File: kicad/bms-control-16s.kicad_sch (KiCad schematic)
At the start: 18 parts, among them J1 RJ45, J2 UEXT, J3 USB_B_Micro, J4 RJ45, J5 Conn_02x09_Top_Bottom

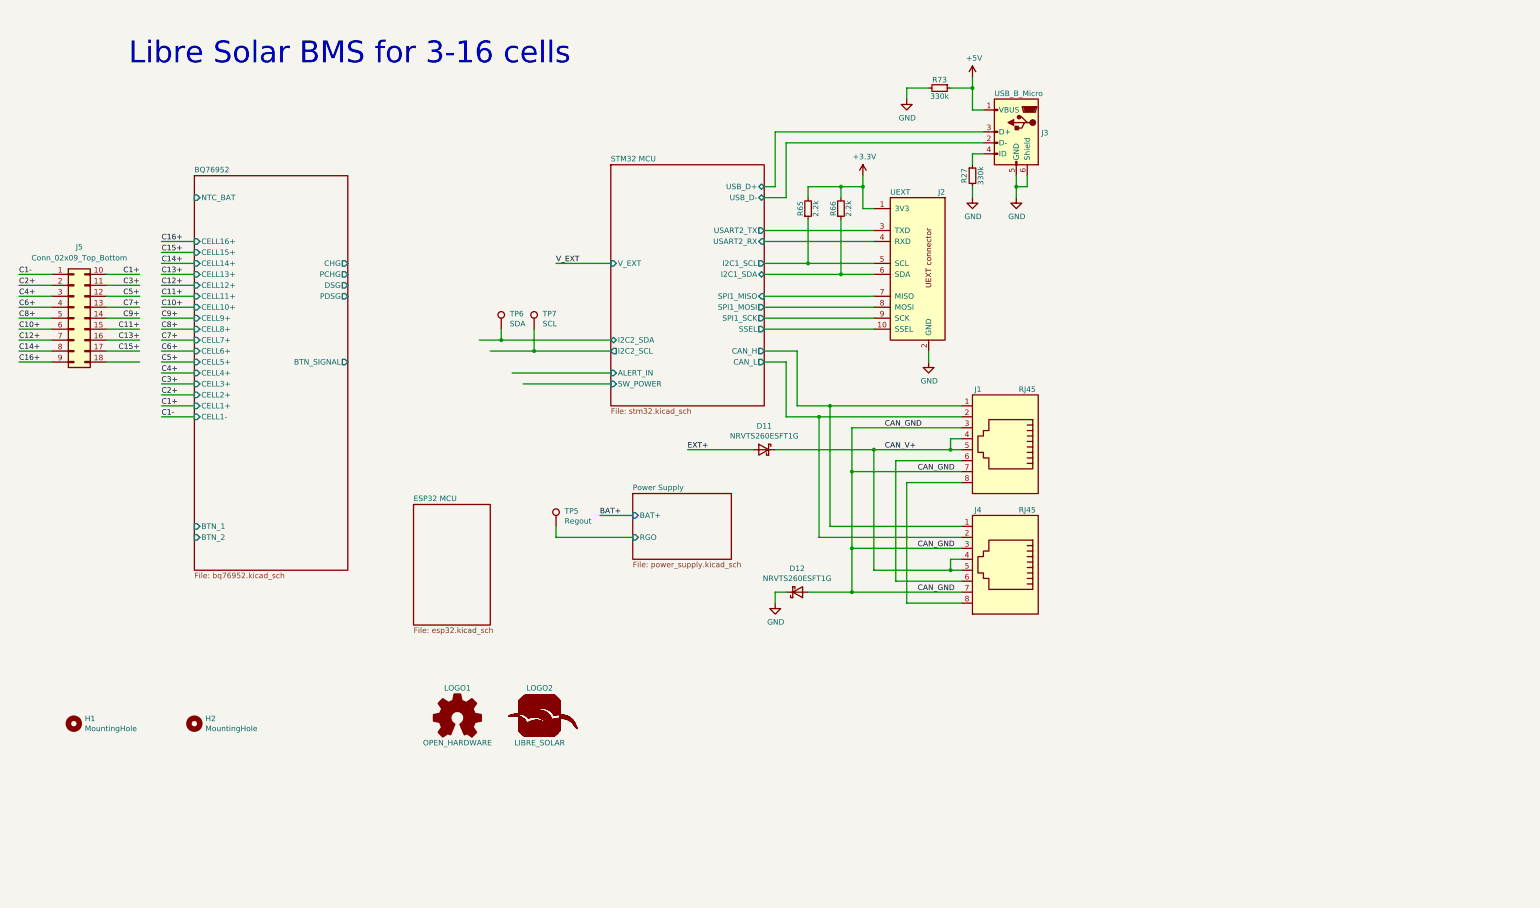
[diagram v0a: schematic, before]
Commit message: Update KiCad files based on spec updates
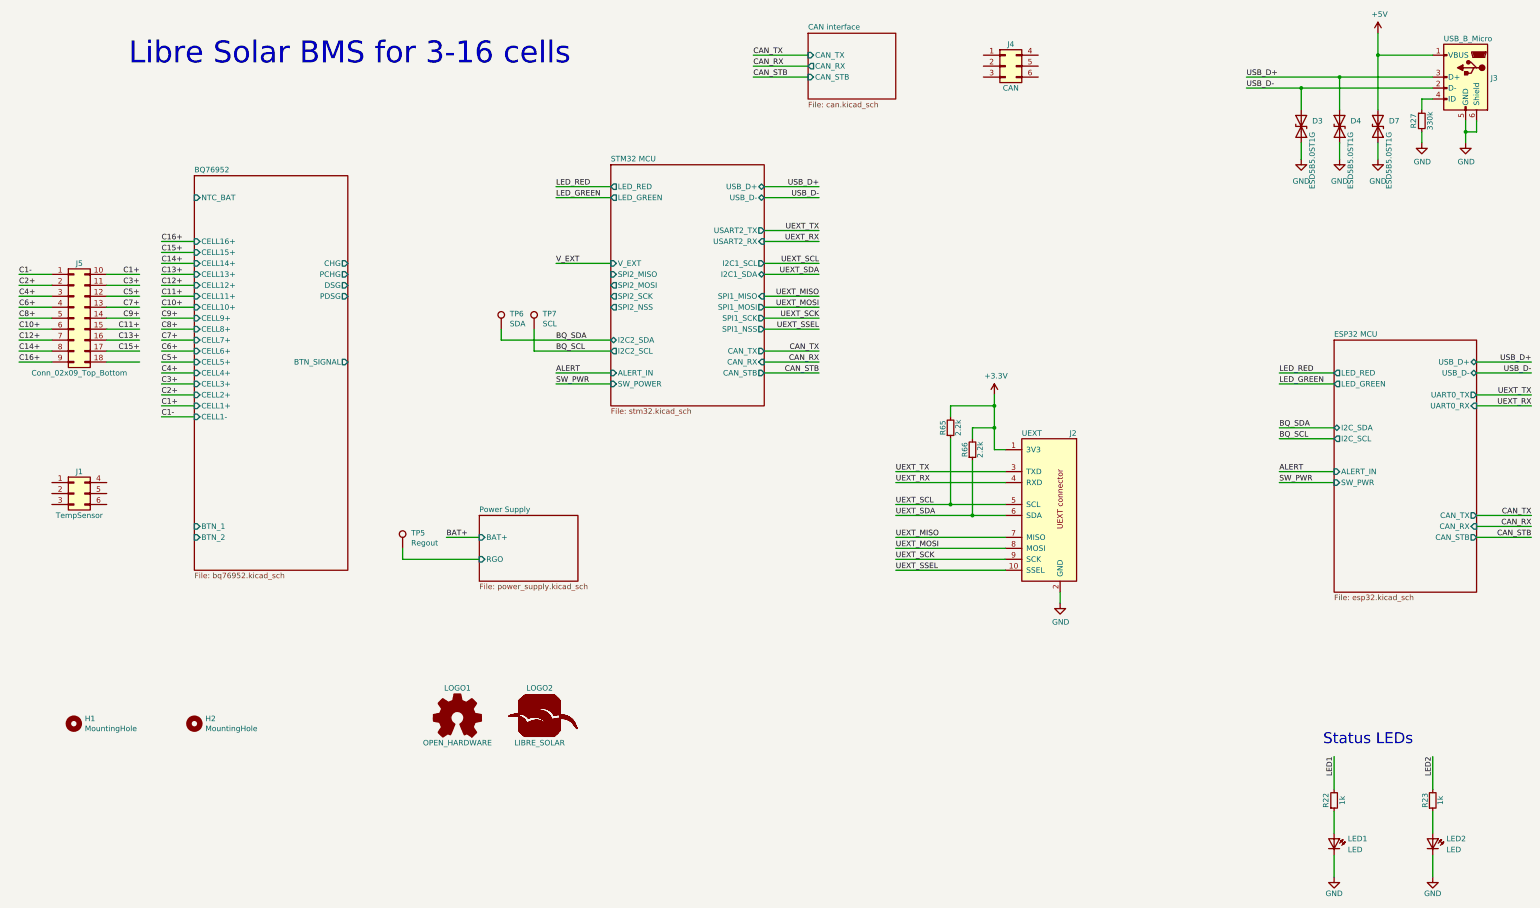
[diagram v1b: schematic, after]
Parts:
- removed D11, D12: NRVTS260ESFT1G, Diode_SMD:D_SOD-123, symbol LibreSolar:D_Schottky
- removed J1, J4: RJ45, LibreSolar:RJ45_8P8C, symbol Connector:8P8C
- removed R73: 330k, LibreSolar:R_0603_1608, symbol LibreSolar:R
- added D3, D4, D7: ESD5B5.0ST1G, Diode_SMD:D_SOD-523, symbol Diode:SZESD9B5.0ST5G
- added J1: TempSensor, Connector_Molex:Molex_Micro-Fit_3.0_43045-0600_2x03_P3.00mm_Horizontal, symbol Connector_Generic:Conn_02x03_Top_Bottom
- added J4: CAN, Connector_Molex:Molex_Micro-Fit_3.0_43045-0600_2x03_P3.00mm_Horizontal, symbol Connector_Generic:Conn_02x03_Top_Bottom
- added LED1, LED2: LED, LED_SMD:LED_0603_1608Metric, symbol bms-control-16s-rescue:D_LED-LibreSolar
- added R22, R23: 1k, LibreSolar:R_0603_1608, symbol LibreSolar:R
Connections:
- net +5V: now also D7.2 (A2)
- net GND: now also D3.1 (A1), D4.1 (A1), D7.1 (A1), LED1.1 (K), LED2.1 (K)
- net STM32 MCU/I2C1_SCL renamed UEXT_SCL
- net STM32 MCU/I2C1_SDA renamed UEXT_SDA
- net STM32 MCU/I2C2_SCL renamed BQ_SCL
- net STM32 MCU/I2C2_SDA renamed BQ_SDA
- net STM32 MCU/SPI1_MISO renamed UEXT_MISO
- net STM32 MCU/SPI1_MOSI renamed UEXT_MOSI
- net STM32 MCU/SPI1_SCK renamed UEXT_SCK
- net STM32 MCU/SSEL renamed UEXT_SSEL
- net STM32 MCU/USART2_RX renamed UEXT_RX
- net STM32 MCU/USART2_TX renamed UEXT_TX
- net STM32 MCU/USB_D+ renamed USB_D+
- net USB_D+: now also D4.2 (A2)
- net STM32 MCU/USB_D- renamed USB_D-
- net USB_D-: now also D3.2 (A2)
- new net: LED1.2 (A), R22.1
- new net: LED2.2 (A), R23.1
- new net LED1: R22.2
- new net LED2: R23.2
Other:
- added sheet CAN interface (can.kicad_sch)
- sheet ESP32 MCU ports: added ALERT_IN, CAN_RX, CAN_STB, CAN_TX, I2C_SCL, I2C_SDA, LED_GREEN, LED_RED, SW_PWR, UART0_RX, UART0_TX, USB_D+, USB_D-; removed none
- sheet STM32 MCU ports: added CAN_RX, CAN_STB, CAN_TX, LED_GREEN, LED_RED, SPI1_NSS, SPI2_MISO, SPI2_MOSI, SPI2_NSS, SPI2_SCK; removed CAN_H, CAN_L, SSEL
- note added: "Status LEDs"
- moved on the sheet: J2, J3, R27, R65, R66, TP5

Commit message: WIP: Schematic almost finished
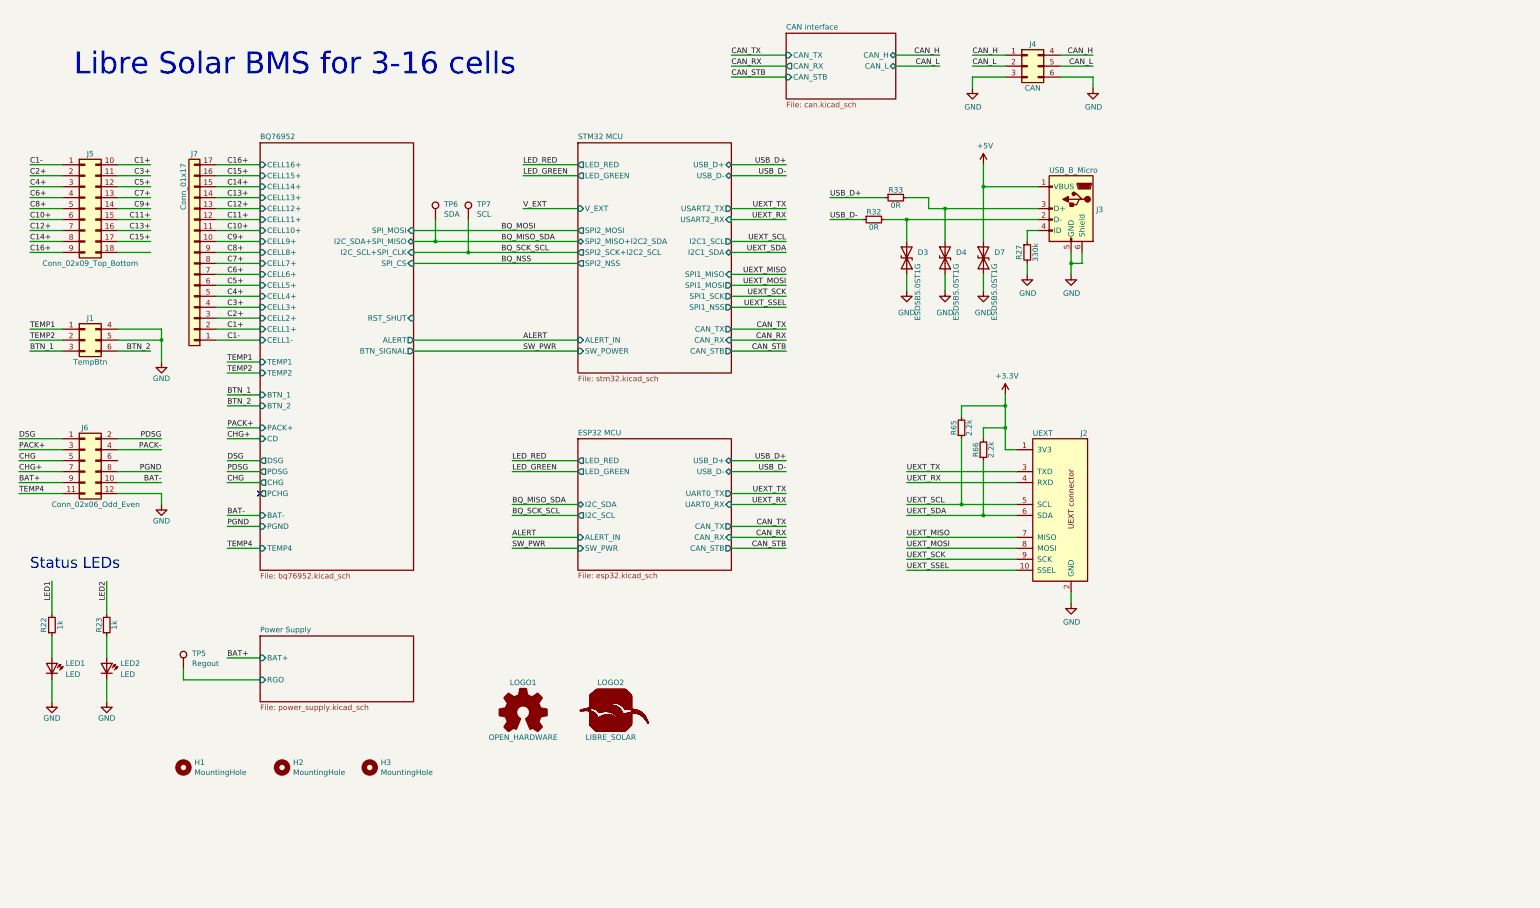
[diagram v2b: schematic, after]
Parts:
- added H3: MountingHole, MountingHole:MountingHole_3.2mm_M3_Pad, symbol Mechanical:MountingHole
- added J6: Conn_02x06_Odd_Even, Connector_PinSocket_2.54mm:PinSocket_2x06_P2.54mm_Vertical, symbol Connector_Generic:Conn_02x06_Odd_Even
- added J7: Conn_01x17, Connector_PinHeader_2.54mm:PinHeader_1x17_P2.54mm_Vertical, symbol Connector_Generic:Conn_01x17
- added R32, R33: 0R, LibreSolar:R_0603_1608, symbol LibreSolar:R
- J1: value TempSensor -> TempBtn
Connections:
- net BAT+: now also J6.9 (Pin_9)
- net C1+: now also J7.2 (Pin_2)
- net C1-: now also J7.1 (Pin_1)
- net C10+: now also J7.11 (Pin_11)
- net C11+: now also J7.12 (Pin_12)
- net C12+: now also J7.13 (Pin_13)
- net C13+: now also J7.14 (Pin_14)
- net C14+: now also J7.15 (Pin_15)
- net C15+: now also J7.16 (Pin_16)
- net C16+: now also J7.17 (Pin_17)
- net C2+: now also J7.3 (Pin_3)
- net C3+: now also J7.4 (Pin_4)
- net C4+: now also J7.5 (Pin_5)
- net C5+: now also J7.6 (Pin_6)
- net C6+: now also J7.7 (Pin_7)
- net C7+: now also J7.8 (Pin_8)
- net C8+: now also J7.9 (Pin_9)
- net C9+: now also J7.10 (Pin_10)
- net GND: now also J1.4 (Pin_4), J1.5 (Pin_5), J4.3 (Pin_3), J4.6 (Pin_6), J6.12 (Pin_12)
- net USB_D+: now also R33.1; no longer D4.2 (A2), J3.3 (D+)
- net USB_D-: now also R32.1; no longer D3.2 (A2), J3.2 (D-)
- net CAN_H: now reaches J4.1 (Pin_1)
- net CAN_H: now also J4.4 (Pin_4)
- net CAN_L: now reaches J4.2 (Pin_2)
- net CAN_L: now also J4.5 (Pin_5)
- net TEMP1: now reaches J1.1 (Pin_1)
- net TEMP2: now reaches J1.2 (Pin_2)
- net BTN_1: now reaches J1.3 (Pin_3)
- net BTN_2: now reaches J1.6 (Pin_6)
- net BQ_SCL renamed BQ_SCK_SCL
- net BQ_SDA renamed BQ_MISO_SDA
- new net: D3.2 (A2), J3.2 (D-), R32.2
- new net: D4.2 (A2), J3.3 (D+), R33.2
- new net BAT-: J6.10 (Pin_10)
- new net CHG: J6.5 (Pin_5)
- new net CHG+: J6.7 (Pin_7)
- new net DSG: J6.1 (Pin_1)
- new net PACK+: J6.3 (Pin_3)
- new net PACK-: J6.4 (Pin_4)
- new net PDSG: J6.2 (Pin_2)
- new net PGND: J6.8 (Pin_8)
- new net TEMP4: J6.11 (Pin_11)
- no-connect marks 0 -> 1
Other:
- sheet BQ76952 ports: added ALERT, BAT-, CD, I2C_SCL+SPI_CLK, I2C_SDA+SPI_MISO, PACK+, PGND, RST_SHUT, SPI_CS, SPI_MOSI, TEMP1, TEMP2, TEMP4; removed NTC_BAT
- sheet CAN interface ports: added CAN_H, CAN_L; removed none
- sheet STM32 MCU ports: added SPI2_MISO+I2C2_SDA, SPI2_SCK+I2C2_SCL; removed I2C2_SCL, I2C2_SDA, SPI2_MISO, SPI2_SCK
- moved on the sheet: D3, D4, D7, H1, H2, J1, J2, J3, J4, J5, LED1, LED2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

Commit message: v0.1 design ready for review
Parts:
- removed J1: TempBtn, Connector_Molex:Molex_Micro-Fit_3.0_43045-0600_2x03_P3.00mm_Horizontal, symbol Connector_Generic:Conn_02x03_Top_Bottom
- removed J4: CAN, Connector_Molex:Molex_Micro-Fit_3.0_43045-0600_2x03_P3.00mm_Horizontal, symbol Connector_Generic:Conn_02x03_Top_Bottom
- removed J5: Conn_02x09_Top_Bottom, Connector_Molex:Molex_Micro-Fit_3.0_43045-1800_2x09_P3.00mm_Horizontal, symbol Connector_Generic:Conn_02x09_Top_Bottom
- removed J6: Conn_02x06_Odd_Even, Connector_PinSocket_2.54mm:PinSocket_2x06_P2.54mm_Vertical, symbol Connector_Generic:Conn_02x06_Odd_Even
- removed J7: Conn_01x17, Connector_PinHeader_2.54mm:PinHeader_1x17_P2.54mm_Vertical, symbol Connector_Generic:Conn_01x17
- added FID1, FID2: Fiducial, Fiducial:Fiducial_1mm_Mask2mm, symbol Mechanical:Fiducial
- added J1: MicroFit 2x7, Connector_Molex:Molex_Micro-Fit_3.0_43045-1410_2x07-1MP_P3.00mm_Horizontal, symbol Connector_Generic_MountingPin:Conn_02x07_Top_Bottom_MountingPin
- added J10, J9: Conn_01x06, Connector_PinSocket_2.00mm:PinSocket_1x06_P2.00mm_Vertical, symbol Connector_Generic:Conn_01x06
- added J4: Conn_01x06, LibreSolar:Wuerth_WR-WST_2x03_P2.54_DBG, symbol Connector_Generic:Conn_01x06
- added J5: MicroFit 2x9, Connector_Molex:Molex_Micro-Fit_3.0_43045-1810_2x09-1MP_P3.00mm_Horizontal, symbol Connector_Generic_MountingPin:Conn_02x09_Top_Bottom_MountingPin
- added TP10: CHG, TestPoint:TestPoint_Pad_D1.5mm, symbol Connector:TestPoint
- added TP11: CAN_H, TestPoint:TestPoint_Pad_D1.5mm, symbol Connector:TestPoint
- added TP12: SHUT, TestPoint:TestPoint_Pad_D1.5mm, symbol Connector:TestPoint
- added TP13: ALERT, TestPoint:TestPoint_Pad_D1.5mm, symbol Connector:TestPoint
- added TP14: SW_PWR, TestPoint:TestPoint_Pad_D1.5mm, symbol Connector:TestPoint
- added TP2: CAN_L, TestPoint:TestPoint_Pad_D1.5mm, symbol Connector:TestPoint
- added TP3: REG1, TestPoint:TestPoint_Pad_D1.5mm, symbol Connector:TestPoint
- added TP4: PDSG, TestPoint:TestPoint_Pad_D1.5mm, symbol Connector:TestPoint
- added TP8: DSG, TestPoint:TestPoint_Pad_D1.5mm, symbol Connector:TestPoint
- added TP9: CD, TestPoint:TestPoint_Pad_D1.5mm, symbol Connector:TestPoint
- H1, H2, H3: footprint MountingHole:MountingHole_3.2mm_M3_Pad -> MountingHole:MountingHole_3.2mm_M3
- LED1: symbol bms-control-16s-rescue:D_LED-LibreSolar -> LibreSolar:LED; Manufacturer (none) -> any; Remarks (none) -> red
- LED2: symbol bms-control-16s-rescue:D_LED-LibreSolar -> LibreSolar:LED; Manufacturer (none) -> any; Remarks (none) -> green
- R22, R23: Manufacturer Yageo -> any; PartNumber RC0603FR-071KL -> (none)
- R27: Manufacturer Yageo -> any; PartNumber RC0603FR-07330KL -> (none)
- R65, R66: Manufacturer Yageo -> any; PartNumber RC0603FR-072K2L -> (none)
- TP5: value Regout -> REG1; footprint LibreSolar:TestPoint_1mm_pad -> TestPoint:TestPoint_Pad_D1.5mm
- TP6, TP7: footprint LibreSolar:TestPoint_1mm_pad -> TestPoint:TestPoint_Pad_D1.5mm
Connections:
- net LED1 is gone; now on net LED_RED: R22.2
- net LED2 is gone; now on net LED_GREEN: R23.2
- net +3V3: now also J4.1 (Pin_1)
- net ALERT: now also TP13.1
- net BAT+: now also J9.1 (Pin_1)
- net BAT-: now also J10.5 (Pin_5)
- net BQ76952/RST_SHUT: now also TP12.1
- net BTN_1: now also J1.3 (Pin_3)
- net BTN_2: now also J1.10 (Pin_10)
- net C1+: now also J5.10 (Pin_10)
- net C1-: now also J5.1 (Pin_1)
- net C10+: now also J5.6 (Pin_6)
- net C11+: now also J5.15 (Pin_15)
- net C12+: now also J5.7 (Pin_7)
- net C13+: now also J5.16 (Pin_16)
- net C14+: now also J5.8 (Pin_8)
- net C15+: now also J5.17 (Pin_17)
- net C16+: now also J5.9 (Pin_9)
- net C2+: now also J5.2 (Pin_2)
- net C3+: now also J5.11 (Pin_11)
- net C4+: now also J5.3 (Pin_3)
- net C5+: now also J5.12 (Pin_12)
- net C6+: now also J5.4 (Pin_4)
- net C7+: now also J5.13 (Pin_13)
- net C8+: now also J5.5 (Pin_5)
- net C9+: now also J5.14 (Pin_14)
- net CAN_H: now also J1.13 (Pin_13), J1.14 (Pin_14), TP11.1
- net CAN_L: now also J1.6 (Pin_6), J1.7 (Pin_7), TP2.1
- net CHG: now also J9.3 (Pin_3), TP10.1
- net DSG: now also J10.4 (Pin_4), TP8.1
- net GND: now also J1.1 (Pin_1), J1.2 (Pin_2), J1.5 (Pin_5), J1.MP (MountPin), J4.3 (Pin_3), J5.MP (MountPin), J9.2 (Pin_2), J9.6 (Pin_6)
- net PACK+: now also J10.1 (Pin_1), TP3.1
- net PACK-: now also J10.6 (Pin_6)
- net PDSG: now also J10.3 (Pin_3), TP4.1
- net SW_PWR: now also TP14.1
- net TEMP1: now also J1.9 (Pin_9)
- net TEMP2: now also J1.8 (Pin_8)
- net TEMP4: now also J9.5 (Pin_5)
- net USB_D+: now also D4.2 (A2), J3.3 (D+), R33.2; no longer R33.1
- net USB_D-: now also D3.2 (A2), J3.2 (D-), R32.2; no longer R32.1
- net Power Supply/RGO renamed REG1
- new net CD: J9.4 (Pin_4), TP9.1
- new net DBG_RX: J4.5 (Pin_5)
- new net DBG_TX: J4.6 (Pin_6)
- new net ESP_USB_D+: R33.1
- new net ESP_USB_D-: R32.1
- new net SWCLK: J4.4 (Pin_4)
- new net SWDIO: J4.2 (Pin_2)
- no-connect marks 1 -> 5
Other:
- sheet BQ76952 ports: added PACK-, REG1; removed PCHG, PGND
- sheet Power Supply ports: added EN; removed RGO
- sheet STM32 MCU ports: added BQ_SHUT, SWDCLK, SWDIO, USART1_RX, USART1_TX; removed none
- note removed: "Status LEDs"
- moved on the sheet: D3, D4, D7, J2, J3, LED1, LED2, LOGO1, LOGO2, R22, R23, R27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
